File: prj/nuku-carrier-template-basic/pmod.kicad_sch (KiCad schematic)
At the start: 6 parts, among them J7 PMOD_A, J8 PMOD_B, U10 SRV05-4, U7 SRV05-4, U8 SRV05-4, U9 SRV05-4

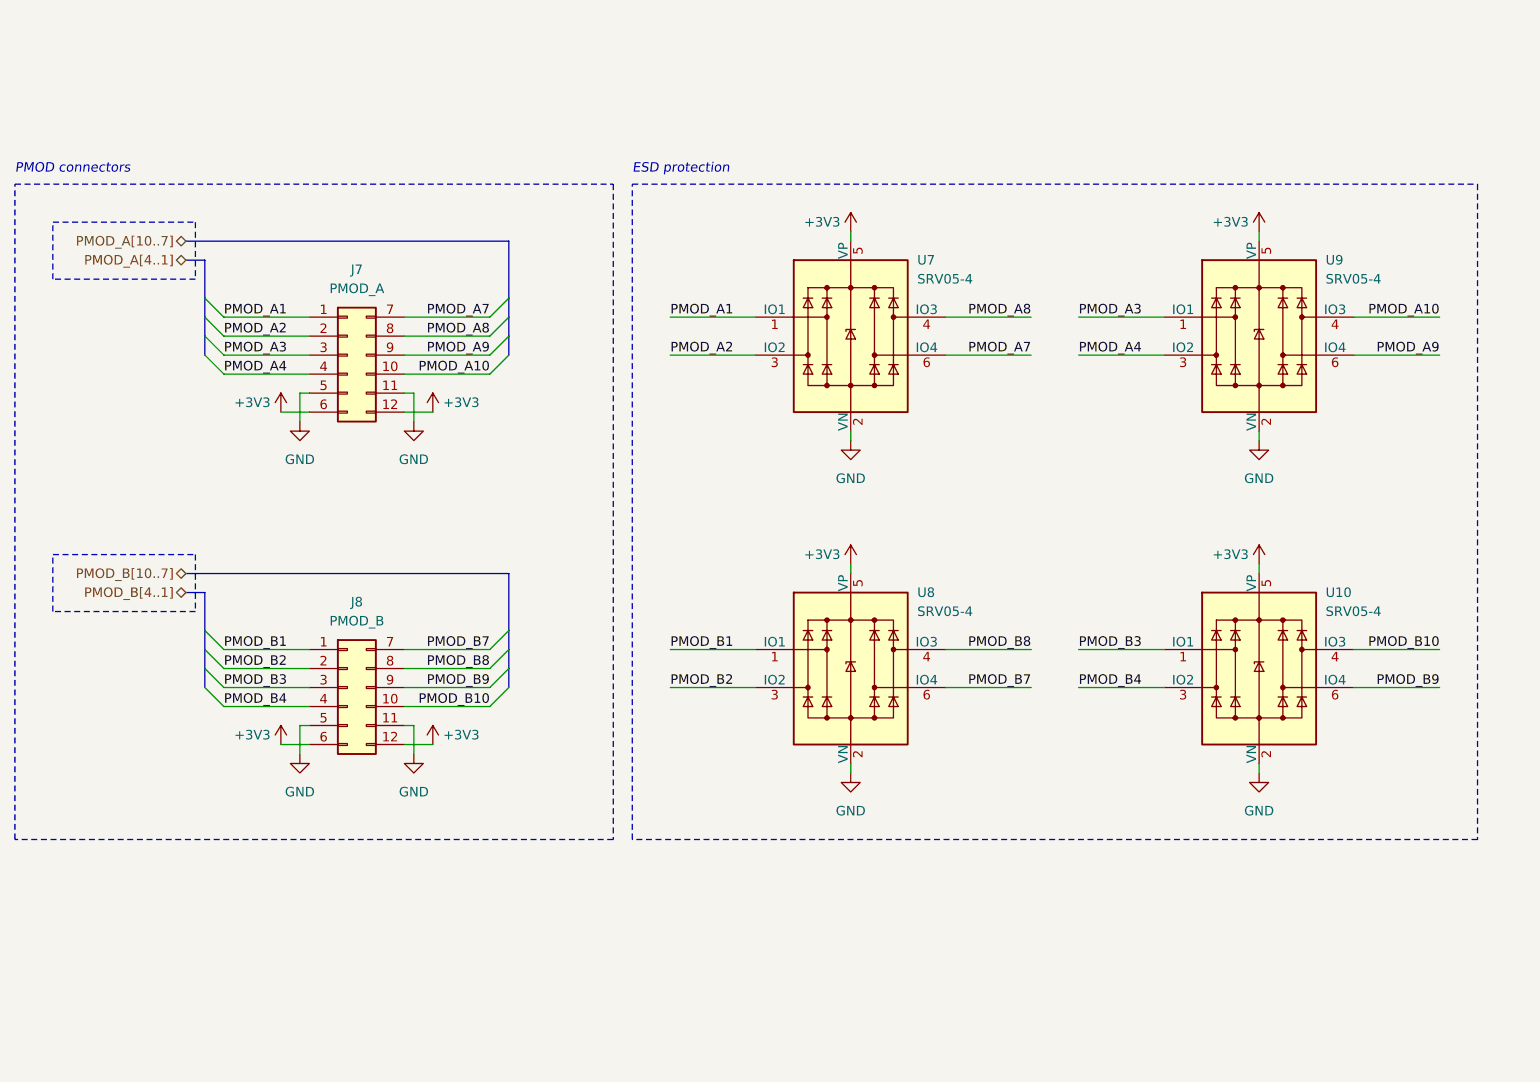
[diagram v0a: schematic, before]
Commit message: Finish template.basic + Production outputs
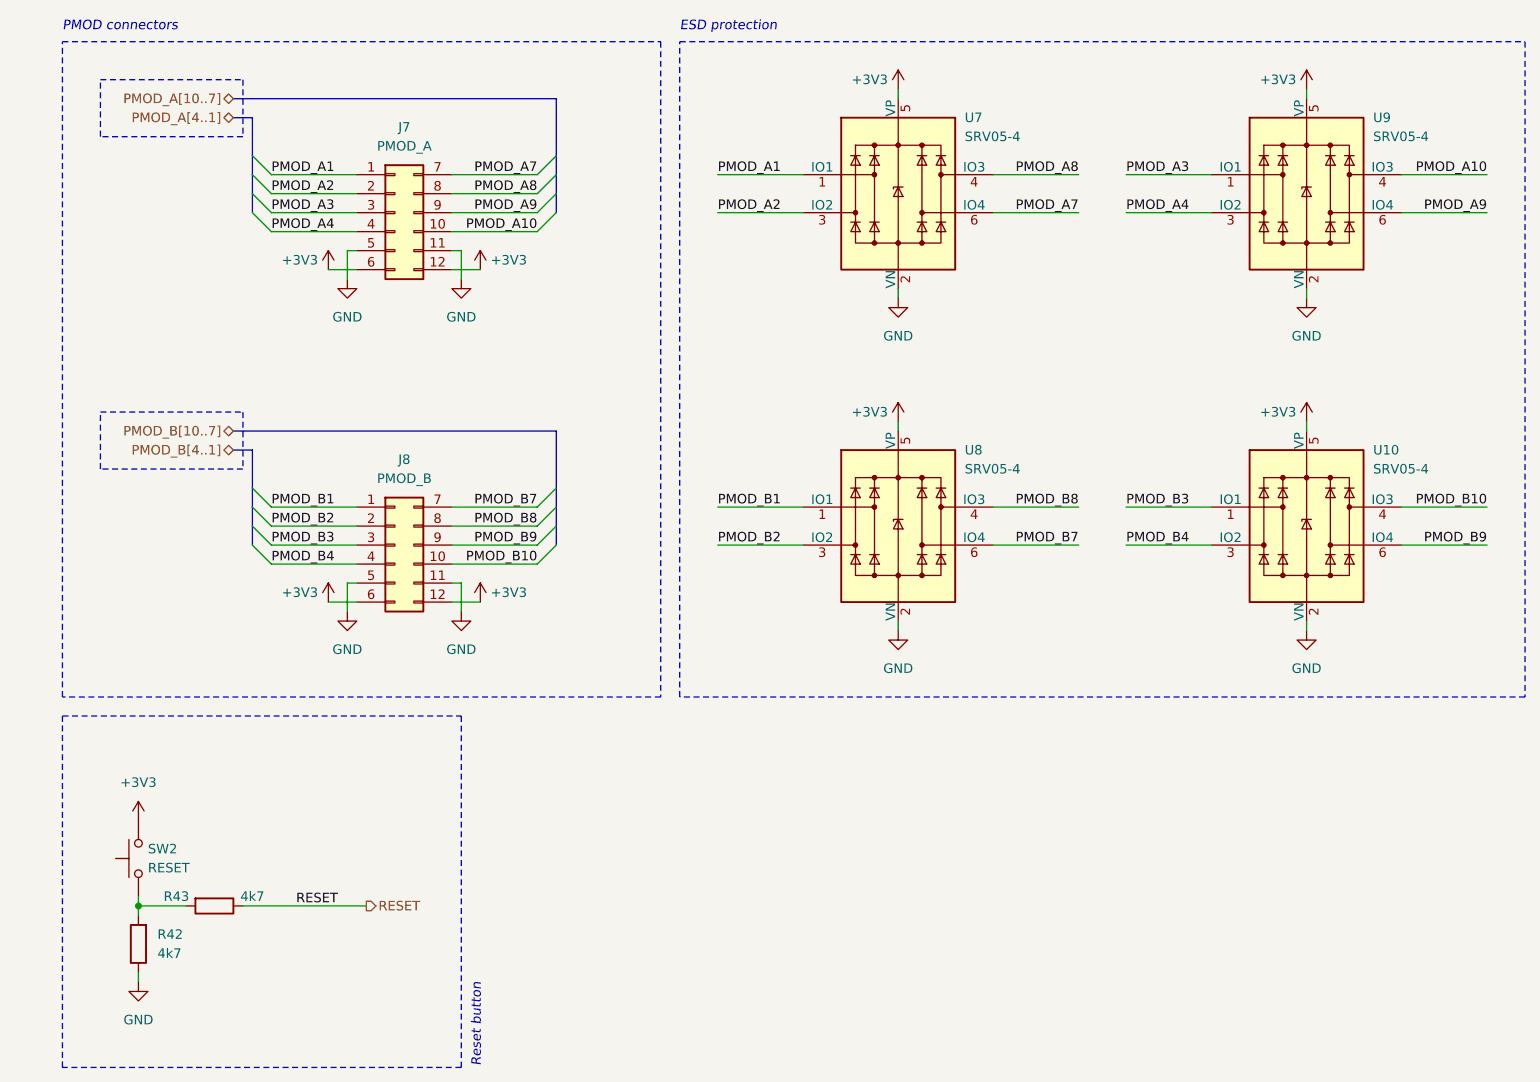
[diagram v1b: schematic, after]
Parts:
- added R42, R43: 4k7, Resistor_SMD:R_0402_1005Metric, symbol Device:R
- added SW2: RESET, nuku:TS-1088-AR02016, symbol Switch:SW_Push
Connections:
- net +3V3: now also SW2.2
- net GND: now also R42.1
- new net: R42.2, R43.2, SW2.1
- new net RESET: R43.1
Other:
- note added: "Reset button"
- moved on the sheet: J7, J8, U10, U7, U8, U9
